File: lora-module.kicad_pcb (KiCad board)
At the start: 4 copper layers, 40 parts, among them U201 STM32WLE5CCUx, U301 BGS12SN6E6327XTSA1, U302 BALFHB-WL-05D3, U401 AT25DF041x-UxN-x

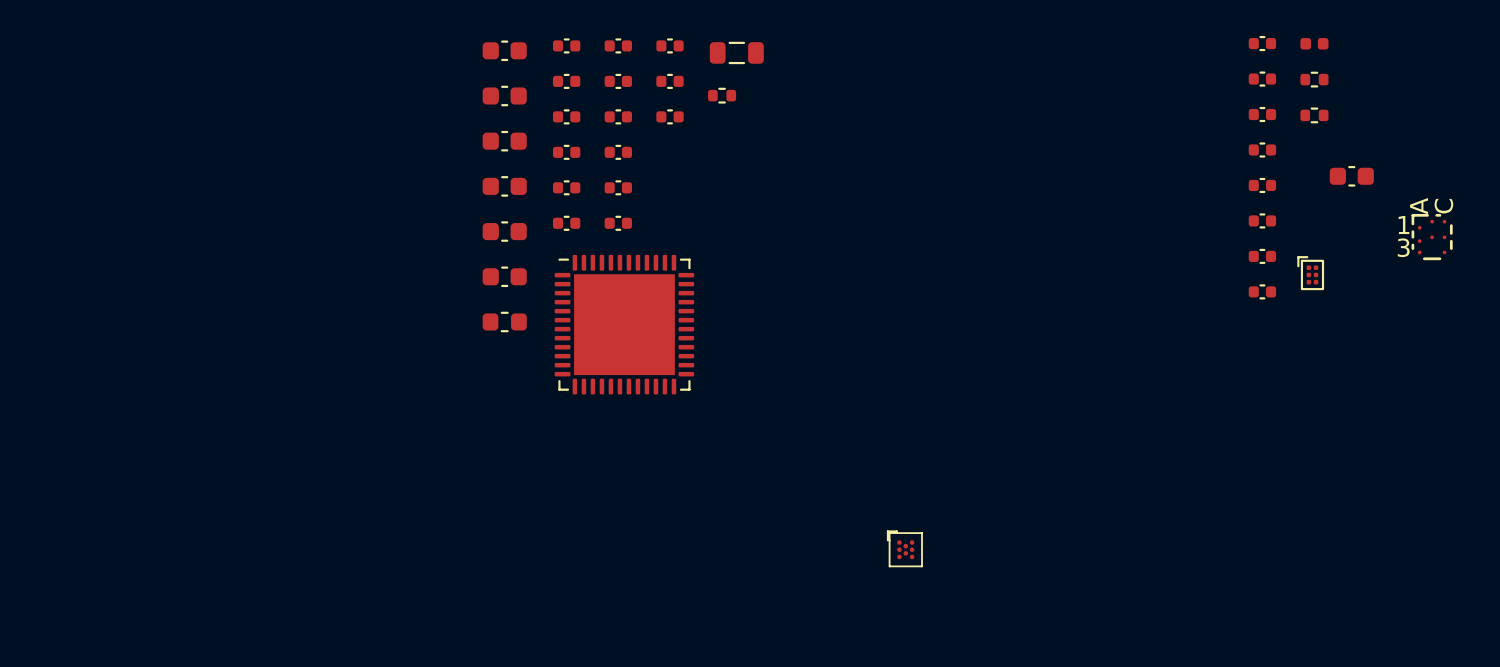
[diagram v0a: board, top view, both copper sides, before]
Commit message: most components placed, routed the RF section
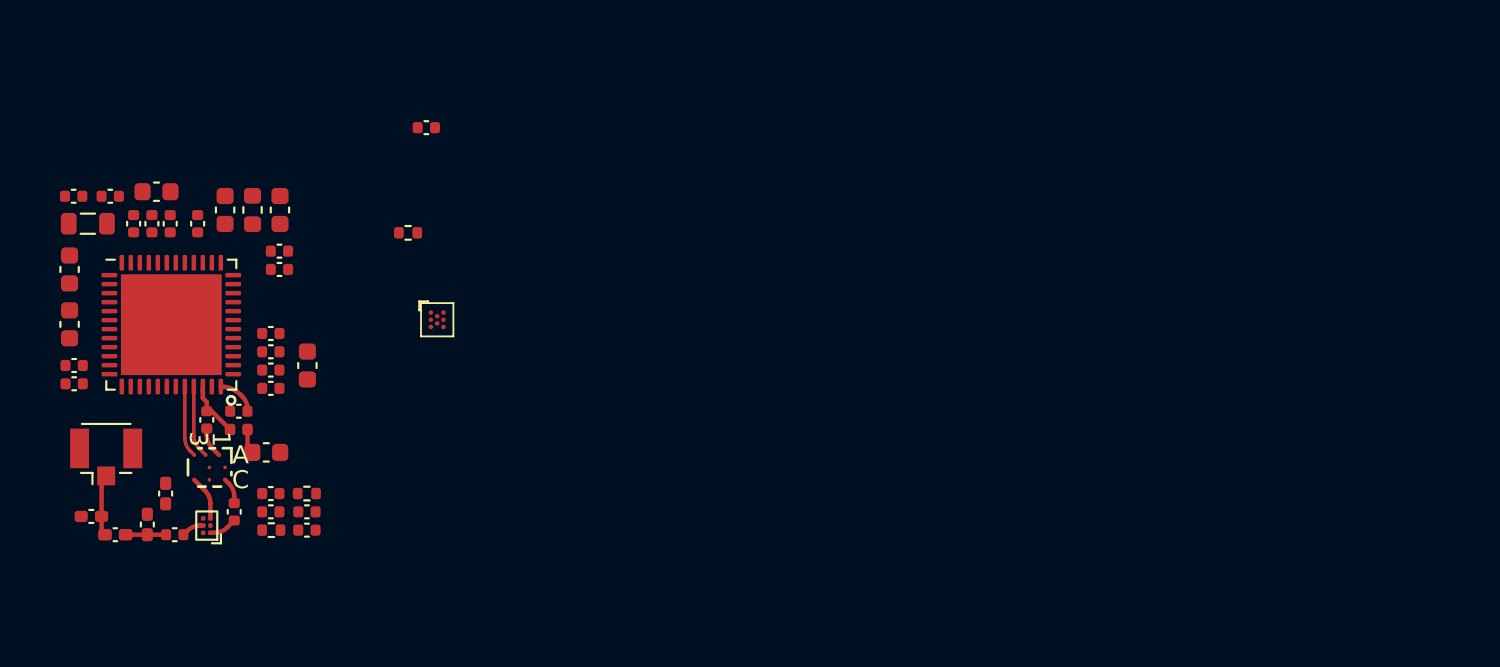
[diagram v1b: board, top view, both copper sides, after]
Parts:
- added C310: 39p, Capacitor_SMD:C_0402_1005Metric, F.Cu at (126.5, 111.5)
- added C311: C, Capacitor_SMD:C_0402_1005Metric_Pad0.74x0.62mm_HandSolder, F.Cu at (125.0, 110.9)
- added C312: C, Capacitor_SMD:C_0402_1005Metric_Pad0.74x0.62mm_HandSolder, F.Cu at (121.9, 110.5)
- added J101: Conn_Coaxial, Connector_Coaxial:U.FL_Hirose_U.FL-R-SMT-1_Vertical, F.Cu at (122.7, 107.2)
- added L302: 0R, Inductor_SMD:L_0402_1005Metric_Pad0.77x0.64mm_HandSolder, F.Cu at (123.2, 111.5)
- C201, C203, C214: value 100n -> 4.7u; footprint Capacitor_SMD:C_0402_1005Metric -> Capacitor_SMD:C_0603_1608Metric
- C205, C210, C220, C221: value 4.7u -> 100n; footprint Capacitor_SMD:C_0603_1608Metric -> Capacitor_SMD:C_0402_1005Metric
- C211: value 100n -> 470n; footprint Capacitor_SMD:C_0402_1005Metric -> Capacitor_SMD:C_0603_1608Metric
- C212: value 470n -> 4.7u
- C215: value 100n -> 33p
- C216: value 33p -> 100n
- C301: value 100p -> 47n; footprint Capacitor_SMD:C_0402_1005Metric -> Capacitor_SMD:C_0603_1608Metric
- C302: value 47n -> 68p; footprint Capacitor_SMD:C_0603_1608Metric -> Capacitor_SMD:C_0402_1005Metric
- C303: value 68p -> 100p
- C304: value 100n -> 39p
- C305: value 1n -> C; footprint Capacitor_SMD:C_0402_1005Metric -> Capacitor_SMD:C_0402_1005Metric_Pad0.74x0.62mm_HandSolder
- C306: value 39p -> 1n
- C307: value C -> 100n
- L201: value 15u -> BK1608HS601-T; footprint Inductor_SMD:L_0805_2012Metric -> Inductor_SMD:L_0603_1608Metric
- L202: value BK1608HS601-T -> 15u; footprint Inductor_SMD:L_0603_1608Metric -> Inductor_SMD:L_0805_2012Metric
- U301: value BGS12SN6E6327XTSA1 -> BALFHB-WL-05D3; footprint lora-module:Infineon_PG-TSNP-6-10_0.7x1.1mm_0.7x1.1mm_P0.4mm -> lora-module:BGA8_BALFHB_STM
- U302: value BALFHB-WL-05D3 -> BGS12SN6E6327XTSA1; footprint lora-module:BGA8_BALFHB_STM -> lora-module:Infineon_PG-TSNP-6-10_0.7x1.1mm_0.7x1.1mm_P0.4mm
- moved U302 69.9 mm to (128.3, 111.0), turned to 180 degrees
- moved C305 63.8 mm to (126.0, 109.2), turned to -90 degrees
- moved L301 63.5 mm to (130.0, 105.7), turned to 180 degrees
- moved C302 63.2 mm to (130.0, 104.6), turned to 180 degrees
- moved R302 62.3 mm to (131.9, 111.3), turned to 180 degrees
- moved U301 62.2 mm to (128.4, 107.8), turned to -90 degrees
- moved C303 61.6 mm to (128.3, 105.1), turned to -90 degrees
- moved C304 61.2 mm to (129.8, 110.2), turned to -90 degrees
- moved R301 60.5 mm to (133.8, 109.2), turned to 180 degrees
- moved C301 59.8 mm to (131.6, 106.9)
- moved C308 56.6 mm to (131.8, 109.2)
- moved C309 56.4 mm to (131.8, 110.2)
- moved C306 56.1 mm to (133.8, 110.2)
- moved C307 55.8 mm to (133.8, 111.3)
- moved C219 33.4 mm to (120.9, 92.7), turned to 180 degrees
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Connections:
- C202 pad 1: VDD -> /STM32WL/VBAT
- C204 pad 1: VDD -> /STM32WL/VBAT
- C206 pad 1: /STM32WL/VBAT -> VDD
- C207 pad 1: /STM32WL/VBAT -> VDD
- C209 pad 1: /STM32WL/VDDA -> VDD
- C210 pad 1: VDD -> /STM32WL/VDDA
- C211 pad 1: VDD -> /STM32WL/VDDPA
- C212 pad 1: /STM32WL/VDDPA -> VDD
- C215 pad 1: VDD -> /STM32WL/VDDPA
- C216 pad 1: /STM32WL/VDDPA -> VDD
- C218 pad 1: /STM32WL/VDDPA -> VDD
- C221 pad 1: VDD -> /STM32WL/VDDPA
- C301 pad 1: /RF frontend/RFO_LP -> /RF frontend/VR_PA
- C301 pad 2: Net-(U302-RFO_IN) -> GND
- C303 pad 1: /RF frontend/VR_PA -> /RF frontend/RFO_LP
- C303 pad 2: GND -> Net-(U301-RFO_IN)
- C304 pad 1: Net-(U301-CTRL) -> Net-(U301-RFO_OUT)
- C304 pad 2: GND -> Net-(U302-RF2)
- C305 pad 1: Net-(U301-CTRL) -> Net-(U301-RFI_IN)
- C306 pad 1: Net-(U302-RFO_OUT) -> Net-(U302-CTRL)
- C306 pad 2: Net-(U301-RF2) -> GND
- C307 pad 1: Net-(U301-RF1) -> Net-(U302-CTRL)
- C308 pad 1: Net-(U301-VDD) -> Net-(U302-VDD)
- C309 pad 1: Net-(U301-VDD) -> Net-(U302-VDD)
- L201 pad 1: /STM32WL/VLXSMPS -> VDD
- L201 pad 2: /STM32WL/VDDPA -> /STM32WL/VDDA
- L202 pad 1: VDD -> /STM32WL/VLXSMPS
- L202 pad 2: /STM32WL/VDDA -> /STM32WL/VDDPA
- R301 pad 2: Net-(U301-CTRL) -> Net-(U302-CTRL)
- R302 pad 1: unconnected-(R302-Pad1) -> VDD
- R302 pad 2: Net-(U301-VDD) -> Net-(U302-VDD)
- U201 pad 20: /STM32WL/RFI_N -> /RF frontend/RFI_P
- U201 pad 21: /STM32WL/RFI_N -> /RF frontend/RFI_N
- U201 pad 22: /STM32WL/RFO_LP -> /RF frontend/RFO_LP
- U201 pad 24: /STM32WL/VR_PA -> /RF frontend/VR_PA
- U201 pad 47: /STM32WL/VLXMPS -> /STM32WL/VLXSMPS
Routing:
- net /RF frontend/RFI_N: track 0.00 -> 4.02 mm
- net /RF frontend/RFI_P: track 0.00 -> 3.97 mm
- net /RF frontend/RF_ANT: track 0.00 -> 3.71 mm
- net /RF frontend/VR_PA: track 0.00 -> 3.62 mm
- net /RF frontend/RFO_LP: track 0.00 -> 3.17 mm
- net Net-(U301-RFI_IN): track 0.00 -> 2.46 mm
- net Net-(C310-Pad2): track 0.00 -> 2.25 mm
- net Net-(U301-RFO_IN): track 0.00 -> 1.70 mm
- net Net-(U302-RF2): track 0.00 -> 1.56 mm
- net Net-(U301-RFO_OUT): track 0.00 -> 1.46 mm
- net Net-(U302-RF): track 0.00 -> 1.26 mm
- net GND: track 0.00 -> 0.63 mm, vias 0 -> 1

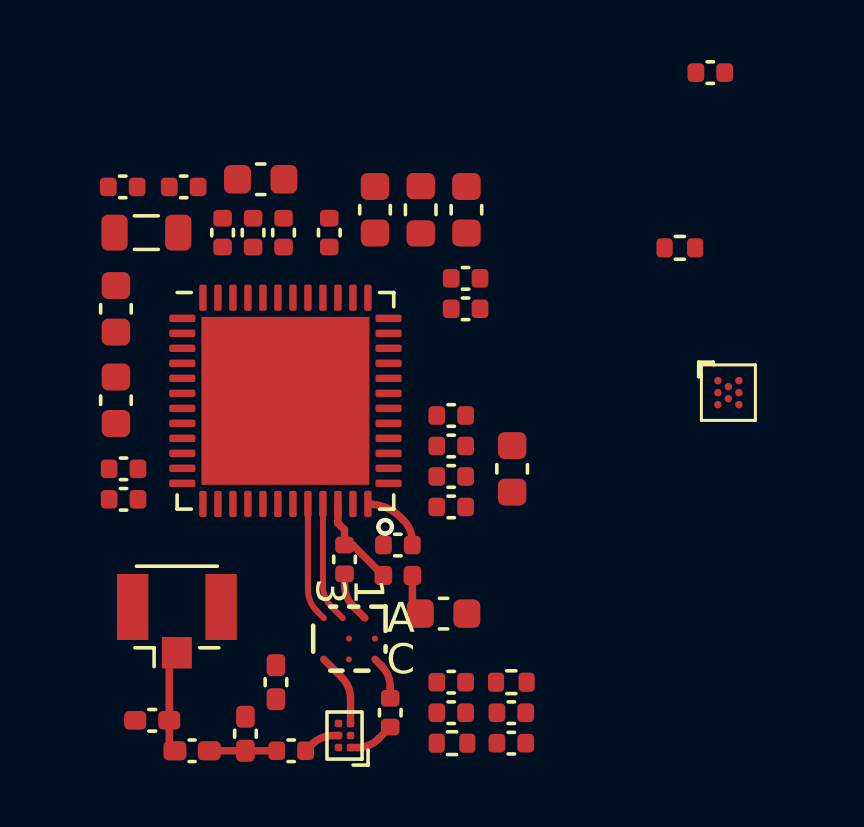
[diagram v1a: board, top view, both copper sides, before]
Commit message: most of the components are placed
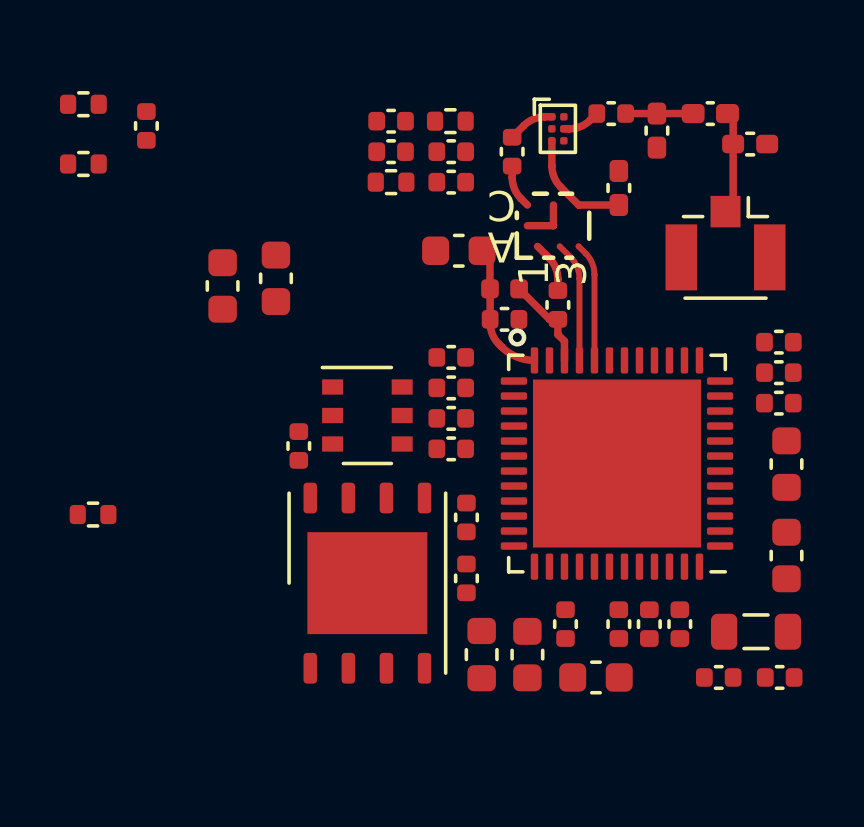
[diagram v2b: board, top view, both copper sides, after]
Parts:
- removed C201: 4.7u, Capacitor_SMD:C_0603_1608Metric
- added C101: 4.7u, Capacitor_SMD:C_0603_1608Metric, F.Cu at (124.2, 96.0)
- added C102: 100n, Capacitor_SMD:C_0402_1005Metric, F.Cu at (121.7, 90.7)
- added C401: 100n, Capacitor_SMD:C_0402_1005Metric, F.Cu at (126.7, 101.3)
- added Q101: PMN48XP, Package_SO:TSOP-6_1.65x3.05mm_P0.95mm, F.Cu at (129.0, 100.3)
- added R101: 1M, Resistor_SMD:R_0402_1005Metric, F.Cu at (119.6, 90.0)
- added R102: 100k, Resistor_SMD:R_0402_1005Metric, F.Cu at (119.6, 91.9)
- U401: value AT25DF041x-UxN-x -> SST26VF080A; footprint Package_CSP:WLCSP-8_1.58x1.63x0.35mm_Layout3x5_P0.35x0.4mm_Ball0.25mm_Pad0.25mm_NSMD -> Package_DFN_QFN:WDFN-8-1EP_6x5mm_P1.27mm_EP3.4x4mm
- moved C312 27.7 mm to (141.8, 91.3), turned to 0 degrees
- moved L302 27.4 mm to (140.5, 90.3), turned to 0 degrees
- moved C219 27.3 mm to (142.8, 109.1), turned to 0 degrees
- moved C311 24.3 mm to (138.7, 90.8), turned to -90 degrees
- moved L202 24.3 mm to (142.0, 107.5), turned to 0 degrees
- moved C218 24.2 mm to (140.7, 109.1), turned to 0 degrees
- moved C211 23.8 mm to (143.0, 105.0), turned to 90 degrees
- moved C310 23.8 mm to (137.2, 90.3), turned to 0 degrees
- moved C214 22.5 mm to (143.0, 102.0), turned to -90 degrees
- moved C216 22.2 mm to (142.7, 98.9), turned to 0 degrees
- moved J101 22.2 mm to (141.0, 94.6), turned to -90 degrees
- moved C207 22.0 mm to (142.7, 99.9), turned to 0 degrees
- moved R201 21.5 mm to (119.9, 103.6), turned to 180 degrees
- moved U302 21.4 mm to (135.4, 90.8), turned to 0 degrees
- moved C307 21.1 mm to (129.8, 90.5), turned to 180 degrees
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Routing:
- net GND: track 0.63 -> 2.19 mm
- net Net-(U301-RFI_IN): track 2.46 -> 3.80 mm
- net /RF frontend/VR_PA: track 3.62 -> 4.63 mm

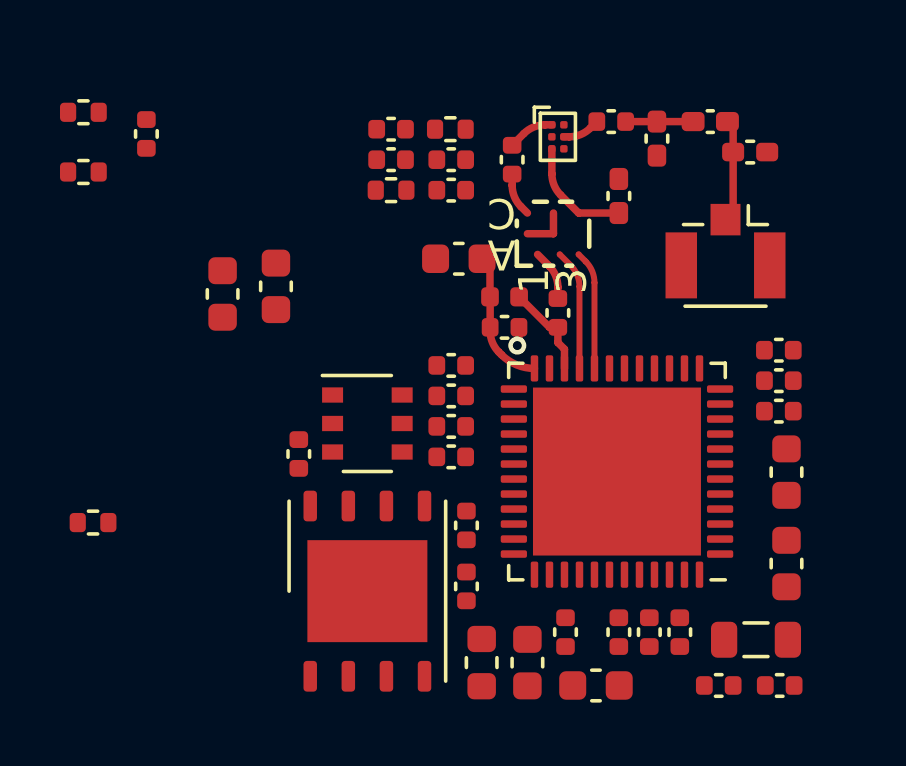
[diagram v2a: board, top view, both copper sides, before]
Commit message: added tag-connect and a led, noticed i forgot a crystal
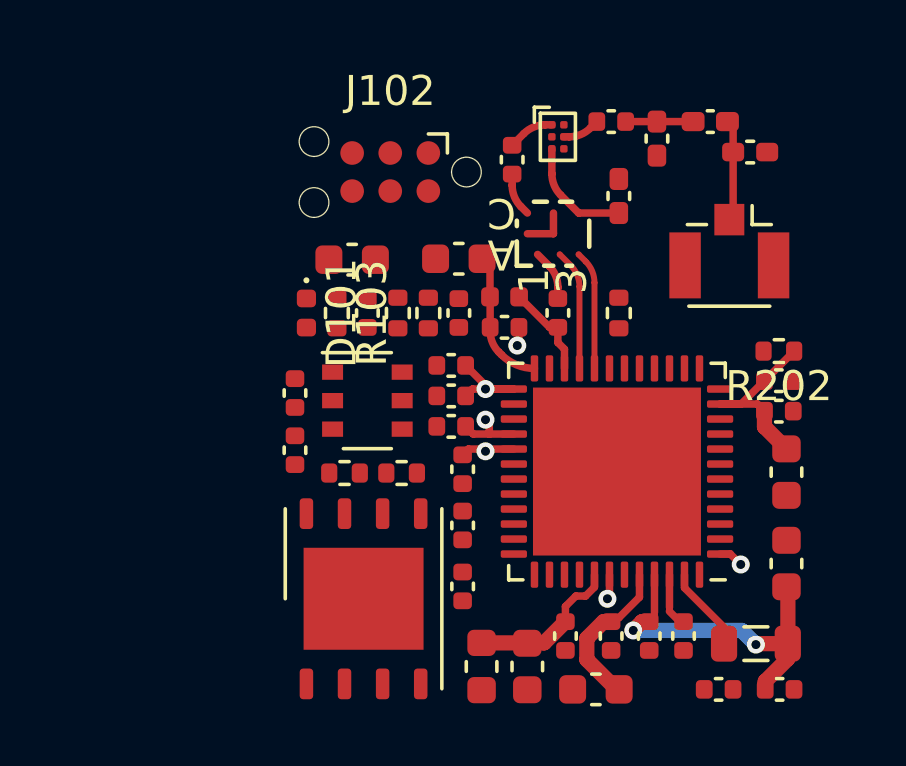
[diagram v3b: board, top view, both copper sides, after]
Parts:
- removed C205: 100n, Capacitor_SMD:C_0402_1005Metric
- removed C212: 4.7u, Capacitor_SMD:C_0603_1608Metric
- removed C306, C308: 1n, Capacitor_SMD:C_0402_1005Metric
- added D101: LED, LED_SMD:LED_0402_1005Metric, F.Cu at (127.0, 96.6)
- added J102: Conn_ARM_SWD_TagConnect_TC2030-NL, Connector:Tag-Connect_TC2030-IDC-NL_2x03_P1.27mm_Vertical, F.Cu at (129.8, 91.9)
- added R103: 10k, Resistor_SMD:R_0402_1005Metric, F.Cu at (128.0, 96.6)
- added R202: 10k, Resistor_SMD:R_0402_1005Metric, F.Cu at (142.7, 97.9)
- moved R201 18.9 mm to (137.4, 96.6), turned to 90 degrees
- moved R101 14.8 mm to (128.3, 102.0), turned to 180 degrees
- moved R102 14.6 mm to (130.2, 102.0)
- moved C102 9.96 mm to (126.6, 99.3)
- moved C307 6.18 mm to (129.0, 96.6), turned to -90 degrees
- moved R302 6.17 mm to (131.1, 96.6), turned to 90 degrees
- moved C309 5.12 mm to (132.1, 96.6), turned to -90 degrees
- moved C101 4.47 mm to (128.5, 94.9), turned to 0 degrees
- moved R301 4.10 mm to (130.0, 96.6), turned to 90 degrees
- moved Q101 0.76 mm to (129.0, 99.6)
- moved C213 0.56 mm to (132.2, 101.9), turned to -90 degrees
- moved C220 0.29 mm to (137.2, 107.4)
- moved U401 0.28 mm to (128.9, 106.2)
- moved C206 0.18 mm to (139.6, 107.4)
- moved C401 0.18 mm to (126.6, 101.2)
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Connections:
- U201 pad 1: unconnected-(U201-PB3-Pad1) -> /STM32WL/SWO
- U201 pad 18: unconnected-(U201-NRST-Pad18) -> /STM32WL/NRST
- U201 pad 36: unconnected-(U201-PA13-Pad36) -> /STM32WL/SWDIO
- U201 pad 42: unconnected-(U201-PA14-Pad42) -> /STM32WL/SWCLK
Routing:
- net /STM32WL/VDDPA: track 0.00 -> 16.8 mm, vias 0 -> 4
- net VDD: track 0.00 -> 15.4 mm, vias 0 -> 1
- net /STM32WL/VDDA: track 0.00 -> 5.24 mm
- net /STM32WL/VLXSMPS: track 0.00 -> 2.72 mm
- net /STM32WL/SWO: track 0.00 -> 0.83 mm, vias 0 -> 1
- net /STM32WL/SWCLK: track 0.00 -> 0.83 mm, vias 0 -> 1
